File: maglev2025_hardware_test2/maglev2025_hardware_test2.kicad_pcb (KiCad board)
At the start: 4 copper layers, 100 x 100 mm, 187 parts, among them J1 SWD, J2 PWRIn, J3 Conn_01x04, J4 Conn_01x04_MountingPin, J5 USB_C_Receptacle_USB2.0, J6 Conn_01x04, J8 Conn_01x07_MountingPin, Q1 AO3400A, SW4 RotaryEncoder_Switch_MP, U1 RY8411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

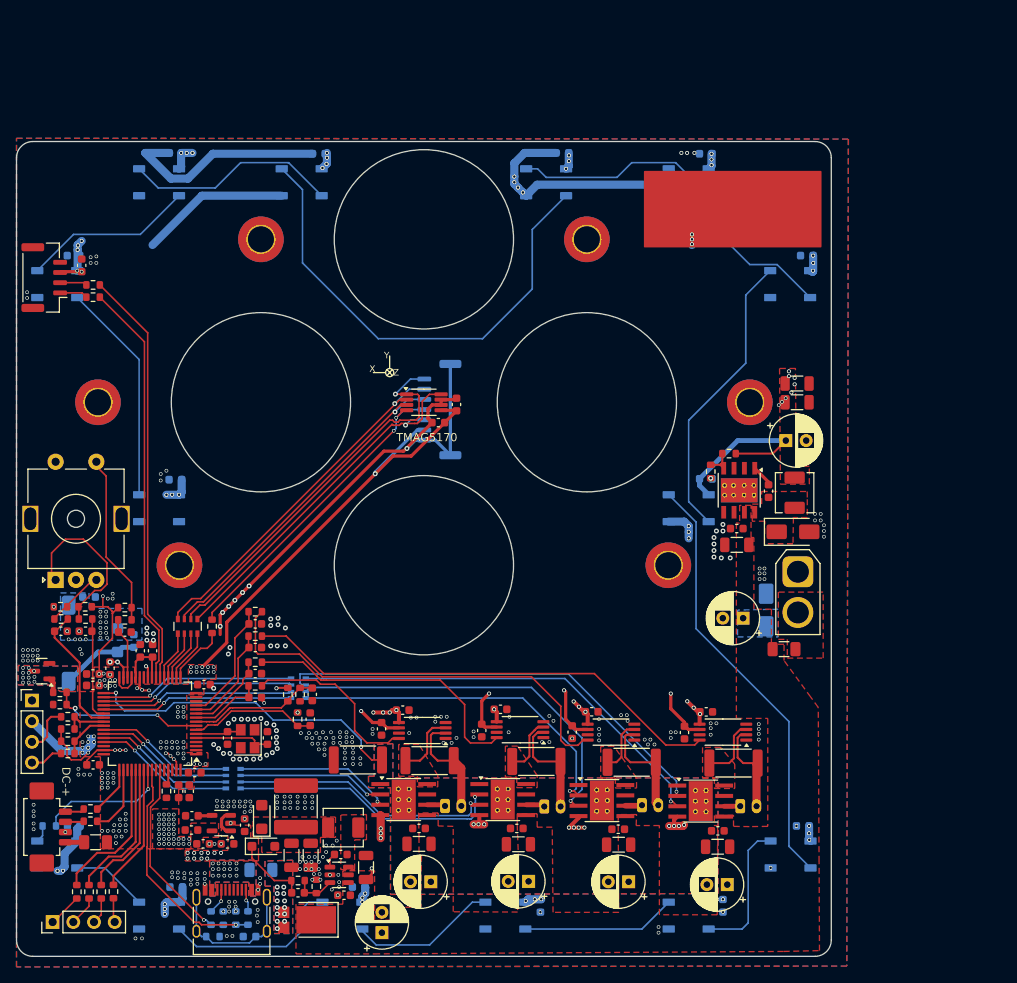
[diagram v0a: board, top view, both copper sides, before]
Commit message: modify layout
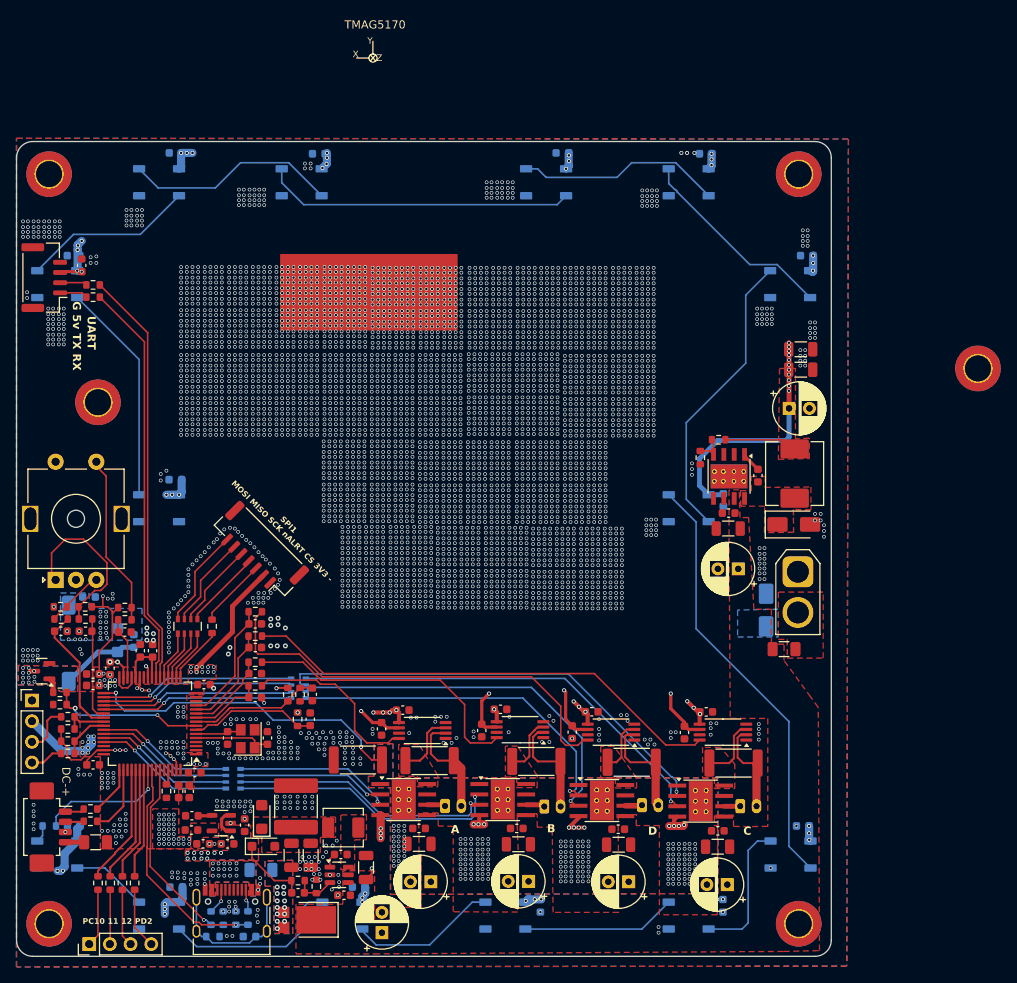
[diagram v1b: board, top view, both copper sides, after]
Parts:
- removed C13, C15: 100n, Capacitor_SMD:C_0603_1608Metric
- removed U2: TMAG5170-Q1, Package_SO:VSSOP-8_3x3mm_P0.65mm
- J8: moved to F.Cu
- L6: footprint Inductor_SMD:L_Sunlord_MWSA0402S -> Inductor_SMD:L_Chilisin_BMRx00060630
- moved H2 46.8 mm to (146.0, 164.0)
- moved H5 46.8 mm to (54.0, 164.0)
- moved H1 28.3 mm to (168.0, 95.8)
- moved J8 28.1 mm to (79.8, 118.2), turned to 135 degrees
- moved H3 27.2 mm to (146.0, 72.0)
- moved H6 27.2 mm to (54.0, 72.0)
- moved C58 6.08 mm to (138.6, 120.5)
- moved J6 5.24 mm to (58.9, 166.5)
- moved C63 4.22 mm to (146.2, 93.5)
- moved C64 4.03 mm to (146.2, 96.0)
- moved C62 3.97 mm to (144.8, 100.8)
- moved C76 3.37 mm to (136.8, 112.0), turned to -90 degrees
- moved R38 2.81 mm to (60.0, 159.0)
- moved R39 2.81 mm to (61.5, 159.0)
- moved R40 2.81 mm to (63.0, 159.0)
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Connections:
- J8 pad 1: SPI1_SCK -> GND
- J8 pad 2: SPI1_MOSI -> +3.3V
- J8 pad 3: SPI1_MISO -> ~{MAG_CS}
- J8 pad 4: ~{MAG_CS} -> ~{MAG_ALRT}
- J8 pad 5: ~{MAG_ALRT} -> SPI1_SCK
- J8 pad 6: +3.3V -> SPI1_MISO
- J8 pad 7: GND -> SPI1_MOSI
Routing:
- net GND: track 167.9 -> 18.6 mm, vias 313 -> 4667
- net +3.3V: track 258.5 -> 217.7 mm, vias 141 -> 140
- net SPI1_SCK: track 48.7 -> 10.5 mm, vias 1 -> 0
- net ~{MAG_ALRT}: track 45.2 -> 9.70 mm, vias 1 -> 0
- net SPI1_MOSI: track 44.2 -> 12.3 mm, vias 1 -> 0
- net SPI1_MISO: track 42.7 -> 11.4 mm, vias 1 -> 0
- net ~{MAG_CS}: track 39.7 -> 8.51 mm, vias 2 -> 0
- net Net-(D16-DOUT): track 60.4 -> 38.2 mm
- net +5V_BLINK: track 425.6 -> 443.0 mm, vias 50 -> 53
- net Net-(J6-Pin_4): track 2.98 -> 7.52 mm
- net Net-(J6-Pin_3): track 3.26 -> 7.09 mm
- net /PC10: track 18.2 -> 14.8 mm
- net /PC11: track 17.4 -> 14.3 mm
- net Net-(J6-Pin_2): track 3.69 -> 6.69 mm
- net Net-(J6-Pin_1): track 4.17 -> 7.12 mm
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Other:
- outline, holes or cut-outs redrawn
- board text added: "A"
- board text added: "B"
- board text added: "C"
- board text added: "D"
- board text added: "G 5v TX RX"
- board text added: "PC10 11 12 PD2"
- board text added: "SPI1 MOSI MISO SCK nALRT CS 3V3 -"
- board text added: "UART"

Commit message: modify layout
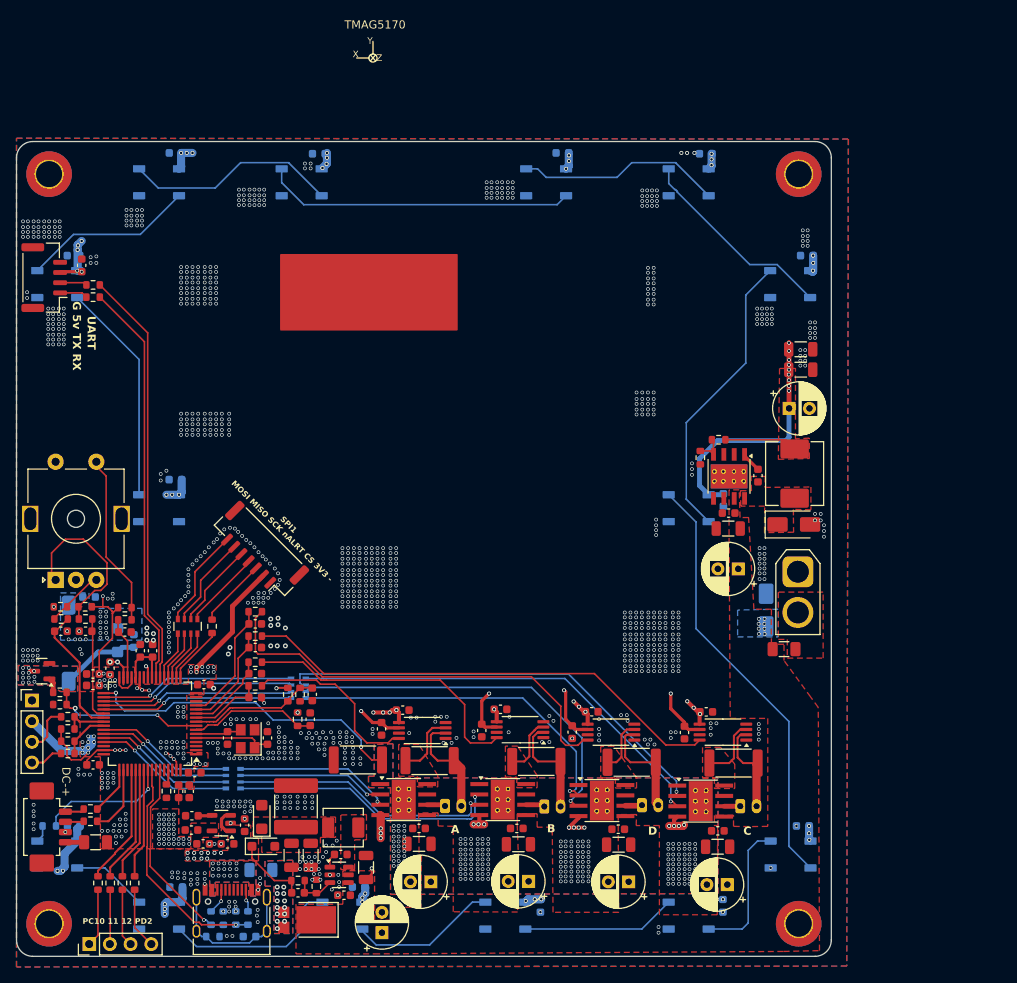
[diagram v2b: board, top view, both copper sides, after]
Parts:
- removed H1, H4: MountingHole_Pad, MountingHole:MountingHole_3.2mm_M3_DIN965_Pad_TopBottom
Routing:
- net VPP: vias 2 -> 10
- net GND: vias 4667 -> 940
- net +5V_BLINK: vias 53 -> 51
